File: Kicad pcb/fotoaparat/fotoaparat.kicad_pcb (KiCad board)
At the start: 2 copper layers, 108 x 67.5 mm, 42 parts, among them J1 Conn_02x01, J2 Conn_01x02_Socket, Q1 BC547, Q2 BC547, Q3 BC547, Q4 BC547, SW1 SW_Push_Dual, U1 TP4056, U10 VBsemi SI2312CDS-T1-GE3, U11 VBsemi SI2312CDS-T1-GE3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

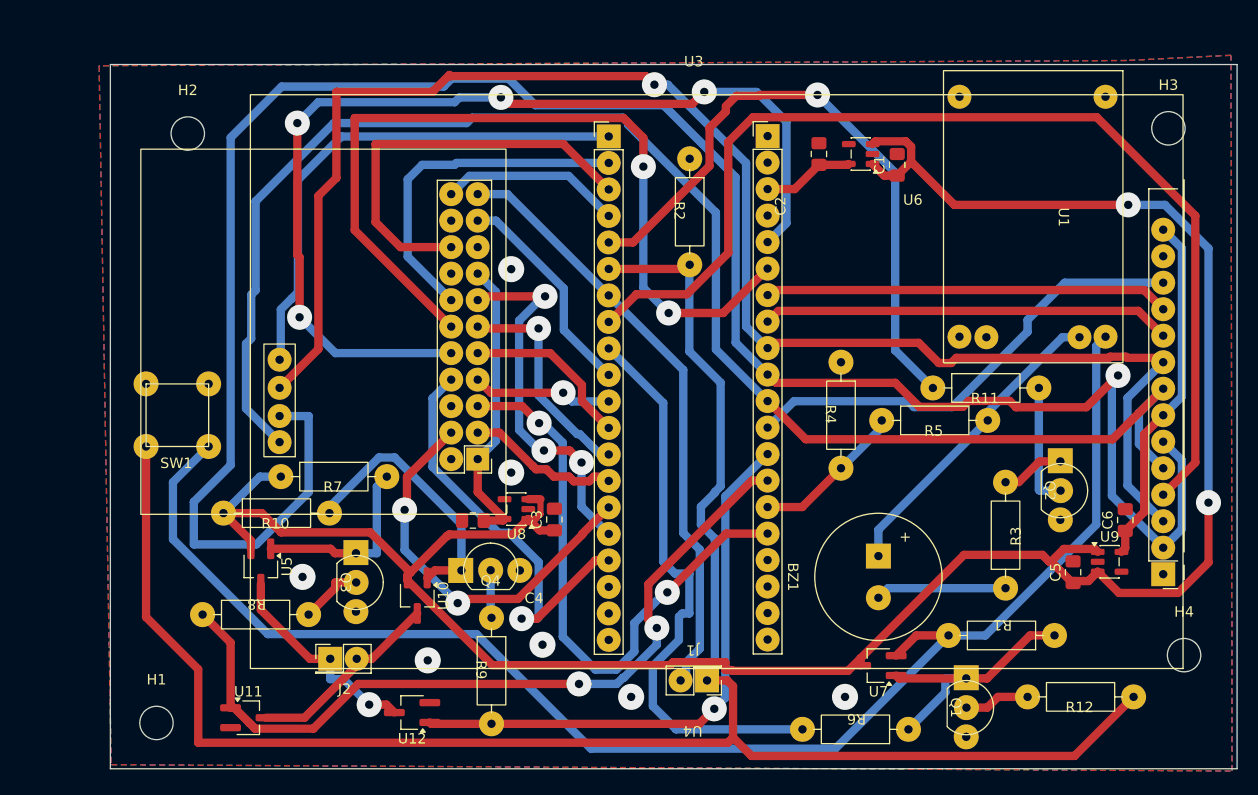
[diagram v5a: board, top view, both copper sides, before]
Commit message: Úprava dps
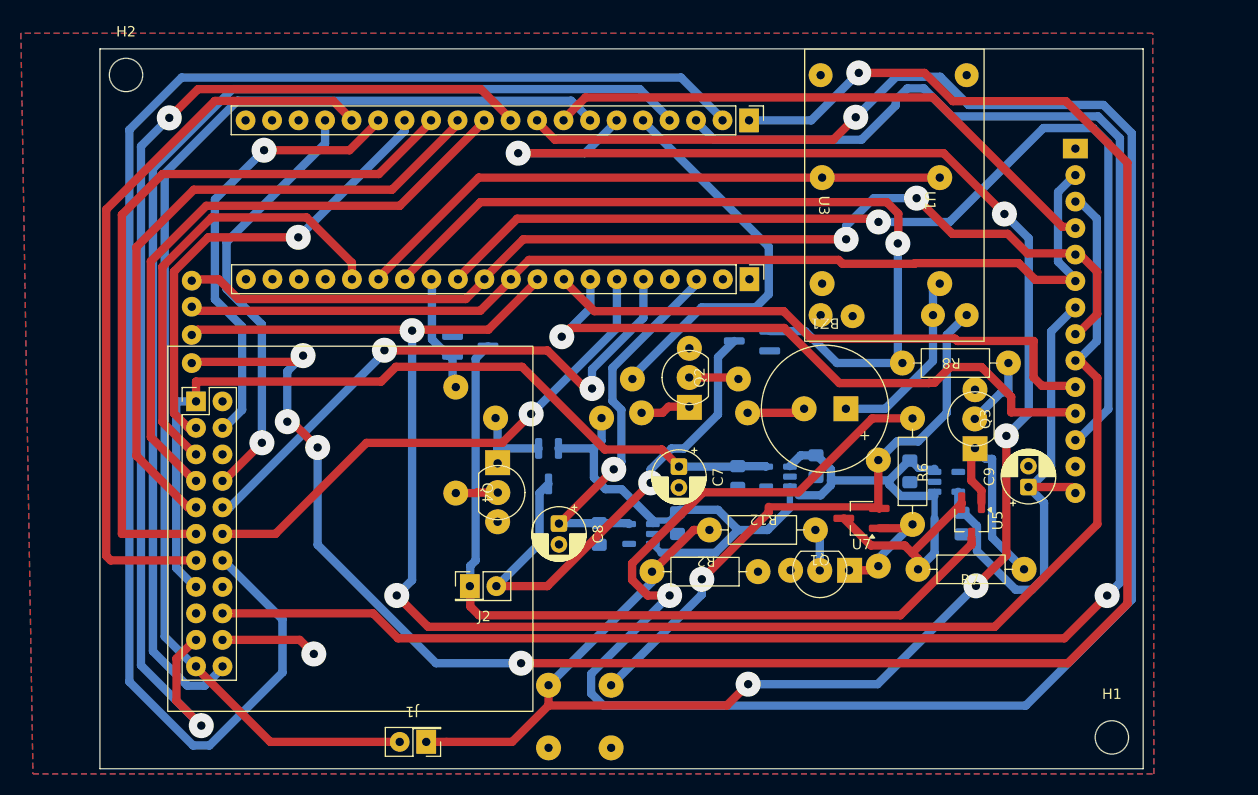
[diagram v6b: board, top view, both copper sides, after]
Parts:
- removed H3, H4: MountingHole, MountingHole:MountingHole_3.2mm_M3
- added C7: 4.7uf, Capacitor_THT:CP_Radial_D5.0mm_P2.00mm, F.Cu at (54.5, -29.0)
- added C8: 4.7uf, Capacitor_THT:CP_Radial_D5.0mm_P2.00mm, F.Cu at (43.0, -23.5)
- added C9: 4.7uf, Capacitor_THT:CP_Radial_D5.0mm_P2.00mm, F.Cu at (88.0, -27.0)
- C1, C2, C3, C4, C5, C6, R1, R10, R11, R3, R4, R5, R9, SW1, U10, U11, U12, U4, U6, U8, U9: moved to B.Cu
- moved H1 91.6 mm to (96.0, -3.00)
- moved R8 71.3 mm to (81.1, -40.4)
- moved U5 68.3 mm to (82.5, -23.8)
- moved Q3 64.3 mm to (84.4, -33.5), turned to 90 degrees
- moved R7 61.7 mm to (82.4, -17.6)
- moved U11 60.3 mm to (61.5, -41.0), turned to 180 degrees
- moved U2 57.4 mm to (6.50, -8.10), turned to 0 degrees
- moved U4 51.8 mm to (94.4, -13.5)
- moved SW1 44.9 mm to (41.9, -8.00)
- moved C2 42.1 mm to (46.9, -22.5), turned to -90 degrees
- moved U6 42.1 mm to (50.9, -22.5)
- moved C1 40.3 mm to (54.4, -23.5), turned to -90 degrees
- moved R12 35.8 mm to (62.6, -24.4), turned to 180 degrees
- moved U12 35.6 mm to (34.5, -40.5), turned to 0 degrees
- moved Q2 34.3 mm to (57.0, -37.5), turned to 90 degrees
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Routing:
- net /pow hold mcu: track 55.4 -> 214.7 mm, vias 0 -> 2
- net /sd cs: track 49.5 -> 199.6 mm, vias 0 -> 5
- net /rck: track 39.9 -> 177.6 mm, vias 0 -> 1
- net +4V: track 220.3 -> 96.2 mm, vias 2 -> 0
- net /d0: track 33.2 -> 146.9 mm
- net /miso: track 205.6 -> 99.7 mm, vias 1 -> 0
- net /rrst: track 17.4 -> 109.1 mm
- net /wr: track 21.0 -> 107.0 mm, vias 0 -> 2
- net /out+: track 141.1 -> 57.3 mm, vias 0 -> 1
- net /rx: track 57.9 -> 115.7 mm
- net Net-(J2-Pin_1): track 20.5 -> 77.5 mm, vias 1 -> 0
- net /lcd cs: track 44.8 -> 98.9 mm, vias 0 -> 1
- net +3.3V ov7670: track 28.1 -> 81.7 mm
- net /d3: track 21.4 -> 71.2 mm, vias 1 -> 0
- net /d5: track 16.4 -> 63.8 mm
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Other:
- board size 108 x 67.5 mm -> 100 x 69 mm

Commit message: Zarovnání
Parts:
- moved BZ1 1.00 mm to (69.5, -43.2)
- moved C1 1.00 mm to (55.4, -23.5)
- moved C2 1.00 mm to (47.9, -22.5)
- moved C3 1.00 mm to (68.6, -29.0)
- moved C4 1.00 mm to (61.1, -28.0)
- moved C5 1.00 mm to (77.6, -28.5)
- moved C6 1.00 mm to (82.6, -23.5)
- moved C7 1.00 mm to (55.5, -29.0)
- moved C8 1.00 mm to (44.0, -23.5)
- moved C9 1.00 mm to (89.0, -27.0)
- moved H1 1.00 mm to (97.0, -3.00)
- moved H2 1.00 mm to (2.50, -66.5)
- moved J1 1.00 mm to (29.9, -5.97)
- moved J2 1.00 mm to (36.8, -14.1)
- moved Q1 1.00 mm to (69.0, -20.5)
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
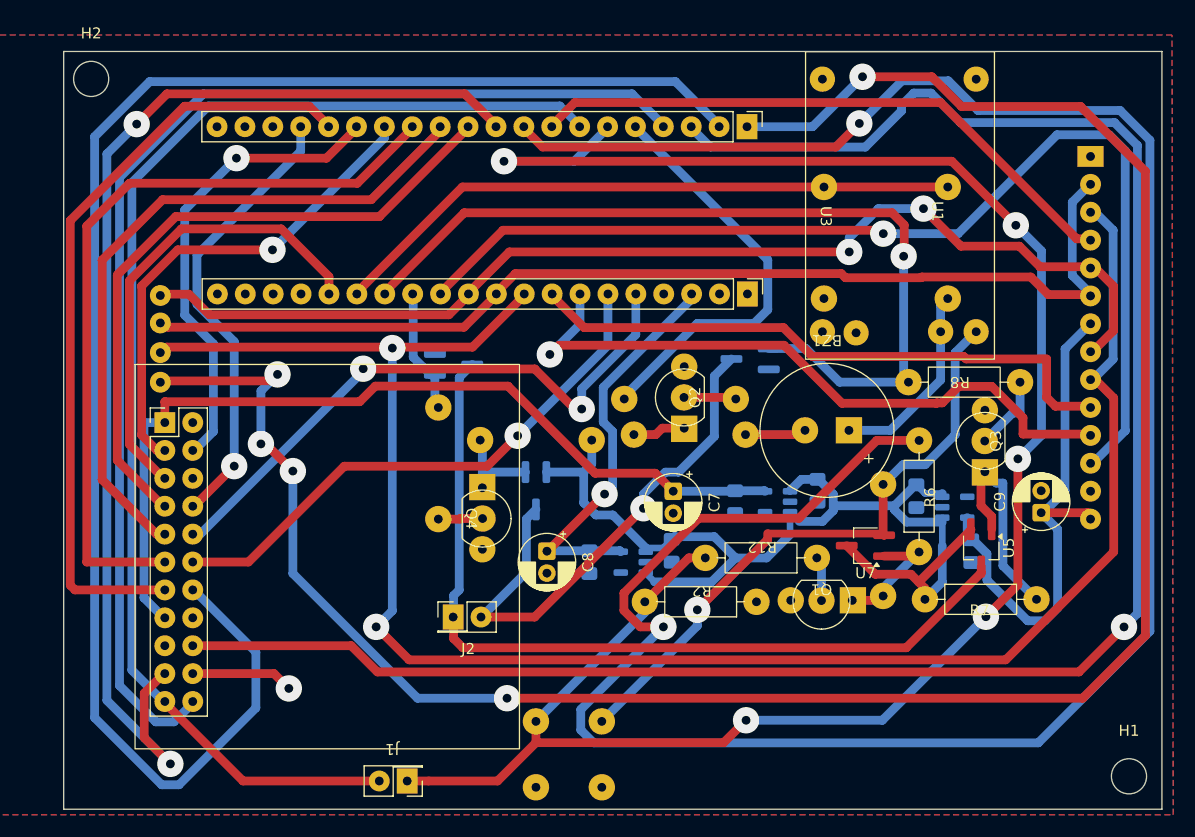
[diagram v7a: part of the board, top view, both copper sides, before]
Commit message: Opačný směr konektoru
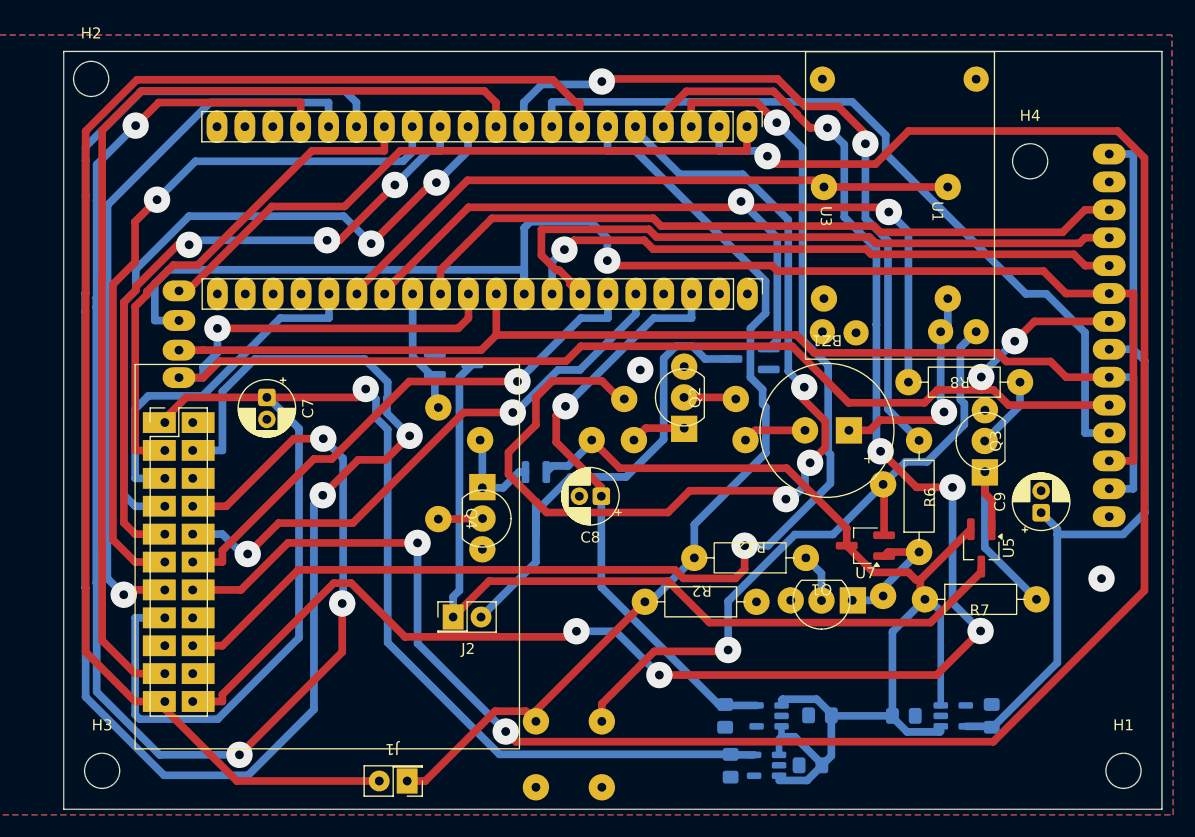
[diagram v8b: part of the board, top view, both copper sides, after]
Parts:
- added H3: MountingHole, MountingHole:MountingHole_3.2mm_M3, F.Cu at (3.50, -3.50)
- added H4: MountingHole, MountingHole:MountingHole_3.2mm_M3, F.Cu at (88.0, -59.0)
- moved C7 38.0 mm to (18.5, -37.5)
- moved C3 25.0 mm to (68.0, -4.00), turned to 180 degrees
- moved U8 24.0 mm to (64.0, -4.00)
- moved C4 24.0 mm to (60.7, -3.96)
- moved C1 20.2 mm to (68.9, -8.55), turned to 180 degrees
- moved C5 20.0 mm to (76.5, -8.50), turned to 0 degrees
- moved U9 19.0 mm to (81.0, -8.50)
- moved C2 18.7 mm to (60.2, -8.50)
- moved U6 18.7 mm to (64.2, -8.50)
- moved C6 15.1 mm to (84.5, -8.50), turned to 90 degrees
- moved C8 7.04 mm to (49.0, -28.5), turned to 180 degrees
- moved U4 4.46 mm to (97.1, -17.6)
- moved R12 1.00 mm to (62.6, -24.4)
- moved H1 0.71 mm to (96.5, -3.50)
- moved R3 0.50 mm to (57.1, -32.1)
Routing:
- net /pow hold mcu: track 214.7 -> 66.2 mm
- net /sd cs: track 199.6 -> 59.2 mm, vias 5 -> 0
- net /siod: track 42.7 -> 166.7 mm, vias 1 -> 2
- net /tx + pow hold: track 181.5 -> 86.4 mm, vias 5 -> 0
- net /d6: track 41.5 -> 134.4 mm, vias 1 -> 4
- net /rck: track 177.6 -> 111.7 mm, vias 1 -> 2
- net /zvuk: track 38.2 -> 92.0 mm, vias 0 -> 3
- net +3.3V ov7670: track 81.7 -> 134.1 mm, vias 0 -> 1
- net /rrst: track 109.1 -> 154.0 mm, vias 0 -> 6
- net /d0: track 146.9 -> 190.1 mm, vias 0 -> 3
- net /mosi: track 167.3 -> 125.0 mm, vias 2 -> 1
- net /clk: track 101.9 -> 136.8 mm, vias 2 -> 3
- net /lcd cs: track 98.9 -> 66.4 mm, vias 1 -> 0
- net +3.3V lcd: track 48.6 -> 71.3 mm
- net +3.3V: track 36.4 -> 54.1 mm
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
